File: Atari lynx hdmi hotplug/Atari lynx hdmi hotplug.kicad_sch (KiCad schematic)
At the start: 9 parts, among them J1 AudioJack3, U1 LM339, U2 4052

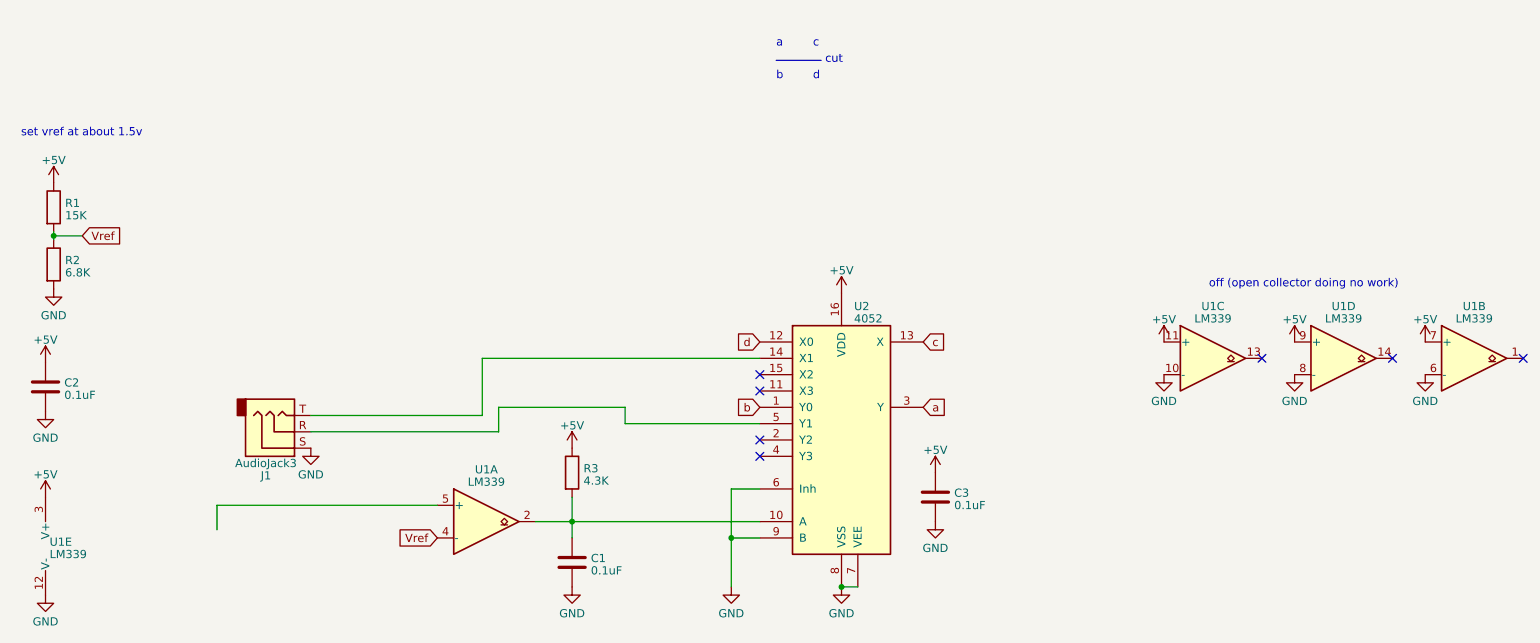
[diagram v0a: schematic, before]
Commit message: updated with amplifier
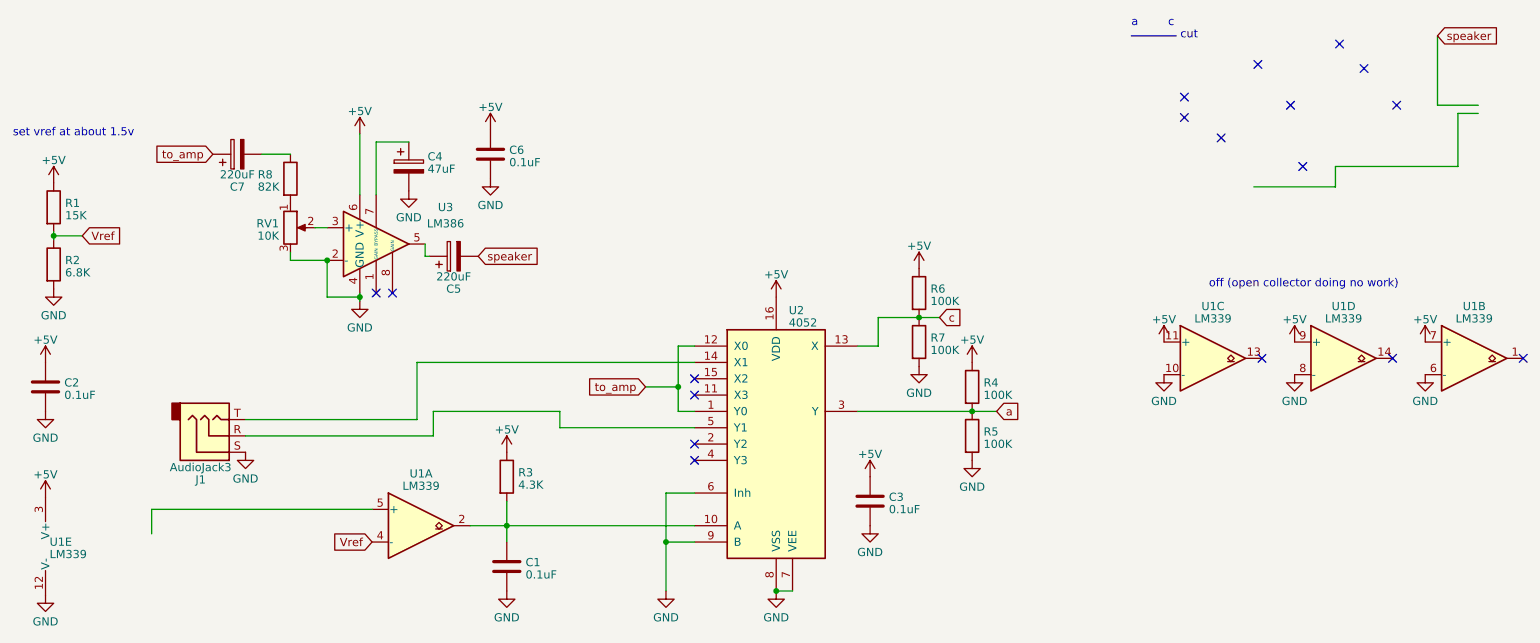
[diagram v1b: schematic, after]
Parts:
- added C4: 47uF, symbol Device:C_Polarized
- added C5, C7: 220uF, symbol Device:C_Polarized
- added C6: 0.1uF, symbol Device:C
- added R4, R5, R6, R7: 100K, symbol Device:R
- added R8: 82K, symbol Device:R
- added RV1: 10K, symbol Device:R_Potentiometer
- added U3: LM386, symbol Amplifier_Audio:LM386
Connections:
- net d is gone; now on net to_amp: U2.12 (X0)
- net +5V: now also C6.1, R4.1, R6.1, U3.6 (V+)
- net GND: now also C4.2, C6.2, R5.2, R7.2, RV1.3, U3.2 (-), U3.4 (GND)
- net a: now also R4.2, R5.1
- net c: now also R6.2, R7.1
- net b renamed to_amp
- net to_amp: now also C7.1
- new net: RV1.2, U3.3 (+)
- new net: C5.1, U3.5
- new net: C4.1, U3.7 (BYPASS)
- new net: C7.2, R8.1
- new net: R8.2, RV1.1
- new net speaker: C5.2
- no-connect marks 7 -> 18
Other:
- note removed: "b"
- note removed: "d"
- moved on the sheet: C1, C3, J1, R3, U1A, U2

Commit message: finished update
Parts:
- removed C7: 220uF, symbol Device:C_Polarized
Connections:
- net to_amp: now also R8.1
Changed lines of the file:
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@@
     )
   )
-  (global_label "to_amp" (shape input) (at 43.815 121.285 180) (fields_autoplaced)
+  (global_label "to_amp" (shape input) (at 51.435 121.285 180) (fields_autoplaced)
     (effects (font (size 1.27 1.27)) (justify right))
-    (property "Intersheetrefs" "${INTERSHEET_REFS}" (at 34.0756 121.285 0)
+    (property "Intersheetrefs" "${INTERSHEET_REFS}" (at 41.6956 121.285 0)
       (effects (font (size 1.27 1.27)) (justify right) hide)
     )
@@
         )
       )
-    )
-  )
-  (symbol (lib_id "Device:C_Polarized") (at 47.625 121.285 90) (unit 1)
-    (in_bom yes) (on_board yes) (dnp no)
-    (property "Reference" "C7" (at 47.625 126.365 90)
-      (effects (font (size 1.27 1.27)))
-    )
-    (property "Value" "220uF" (at 47.625 124.46 90)
-      (effects (font (size 1.27 1.27)))
-    )
-    (property "Footprint" "" (at 51.435 120.3198 0)
-      (effects (font (size 1.27 1.27)) hide)
-    )
-    (property "Datasheet" "~" (at 47.625 121.285 0)
-      (effects (font (size 1.27 1.27)) hide)
-    )
-    (pin "1")
-    (pin "2")
-    (instances
-      (project "Atari lynx hdmi hotplug"
-        (path "/ebabef8d-7cea-423e-ba60-d26ff528317c"
-          (reference "C7") (unit 1)
-        )
-      )
